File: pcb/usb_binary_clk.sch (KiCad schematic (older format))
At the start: 41 parts, among them J1 USB_B_Micro, J2 USB_B_Micro, J3 AVR-ISP-6, SW1 SW_Push, SW2 SW_Push, SW3 SW_Push, U1 MCP7940N-xP, U2 ATtiny84V-10PU, Y1 Crystal

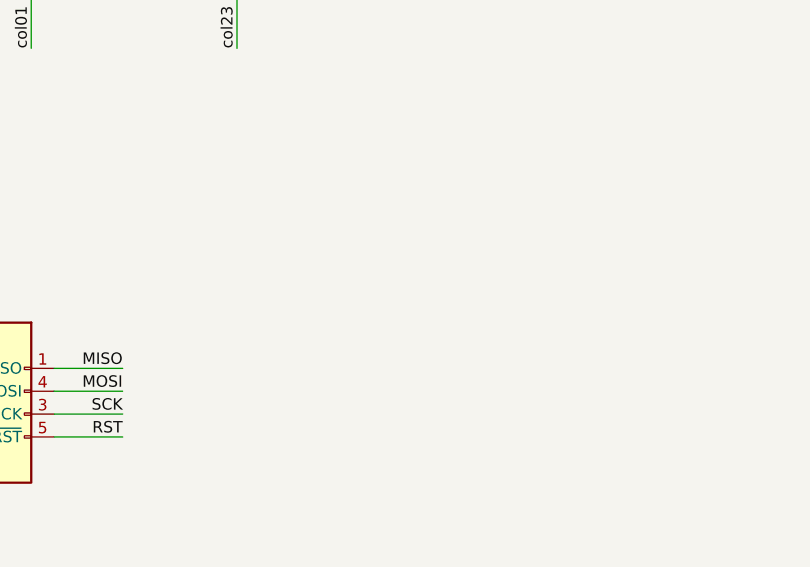
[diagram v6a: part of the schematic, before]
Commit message: add mounting pads for stand/wall mount
fix #7
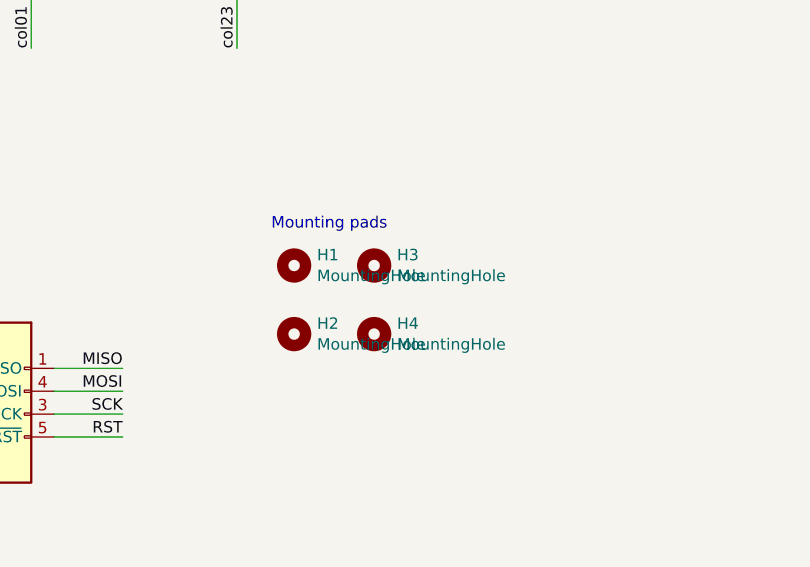
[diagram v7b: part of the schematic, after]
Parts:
- added H1, H2, H3, H4: MountingHole, binary_clk_parts:mountingPad_custom1, symbol Mechanical:MountingHole
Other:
- note added: "Mounting pads"
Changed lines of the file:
@@
 	4900 6950 4600 6950
 $Comp
-L power:+5V #PWR?
+L power:+5V #PWR0121
 U 1 1 61E83871
 P 4100 6200
-F 0 "#PWR?" H 4100 6050 50  0001 C CNN
+F 0 "#PWR0121" H 4100 6050 50  0001 C CNN
 F 1 "+5V" H 4115 6373 50  0000 C CNN
 F 2 "" H 4100 6200 50  0001 C CNN
@@
 	4100 6200 4100 6350
 $Comp
-L power:GND #PWR?
+L power:GND #PWR0122
 U 1 1 61E8E695
 P 4100 7350
-F 0 "#PWR?" H 4100 7100 50  0001 C CNN
+F 0 "#PWR0122" H 4100 7100 50  0001 C CNN
 F 1 "GND" H 4105 7177 50  0000 C CNN
 F 2 "" H 4100 7350 50  0001 C CNN
@@
 Wire Wire Line
 	9850 5350 9550 5350
+$Comp
+L Mechanical:MountingHole H3
+U 1 1 623D2CDE
+P 6000 6200
+F 0 "H3" H 6100 6246 50  0000 L CNN
+F 1 "MountingHole" H 6100 6155 50  0000 L CNN
+F 2 "binary_clk_parts:mountingPad_custom1" H 6000 6200 50  0001 C CNN
+F 3 "~" H 6000 6200 50  0001 C CNN
+	1    6000 6200
+	1    0    0    -1
+$EndComp
+$Comp
+L Mechanical:MountingHole H4
+U 1 1 623D35E7
+P 6000 6500
+F 0 "H4" H 6100 6546 50  0000 L CNN
+F 1 "MountingHole" H 6100 6455 50  0000 L CNN
+F 2 "binary_clk_parts:mountingPad_custom1" H 6000 6500 50  0001 C CNN
+F 3 "~" H 6000 6500 50  0001 C CNN
+	1    6000 6500
+	1    0    0    -1
+$EndComp
+$Comp
+L Mechanical:MountingHole H1
+U 1 1 623D3758
+P 5650 6200
+F 0 "H1" H 5750 6246 50  0000 L CNN
+F 1 "MountingHole" H 5750 6155 50  0000 L CNN
+F 2 "binary_clk_parts:mountingPad_custom1" H 5650 6200 50  0001 C CNN
+F 3 "~" H 5650 6200 50  0001 C CNN
+	1    5650 6200
+	1    0    0    -1
+$EndComp
+$Comp
+L Mechanical:MountingHole H2
+U 1 1 623D391E
+P 5650 6500
+F 0 "H2" H 5750 6546 50  0000 L CNN
+F 1 "MountingHole" H 5750 6455 50  0000 L CNN
+F 2 "binary_clk_parts:mountingPad_custom1" H 5650 6500 50  0001 C CNN
+F 3 "~" H 5650 6500 50  0001 C CNN
+	1    5650 6500
+	1    0    0    -1
+$EndComp
+Text Notes 5550 6050 0    50   ~ 0
+Mounting pads
 $EndSCHEMATC

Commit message: change photodiode footprint to 3mm
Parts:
- D17: footprint custom:LED_D5.0mm -> LED_THT:LED_D3.0mm
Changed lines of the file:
@@
 F 0 "D17" V 1404 6358 50  0000 L CNN
 F 1 "D_Photo" V 1495 6358 50  0000 L CNN
-F 2 "custom:LED_D5.0mm" H 1450 6200 50  0001 C CNN
+F 2 "LED_THT:LED_D3.0mm" H 1450 6200 50  0001 C CNN
 F 3 "~" H 1450 6200 50  0001 C CNN
 	1    1500 6200
